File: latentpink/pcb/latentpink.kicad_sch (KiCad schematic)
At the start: 20 parts, among them M10 WEEE, M3 SCREWHOLE, M4 SCREWHOLE, M5 SCREWHOLE, M6 SCREWHOLE, M7 LONGTHING, M8 OSHW, M9 POLARITY

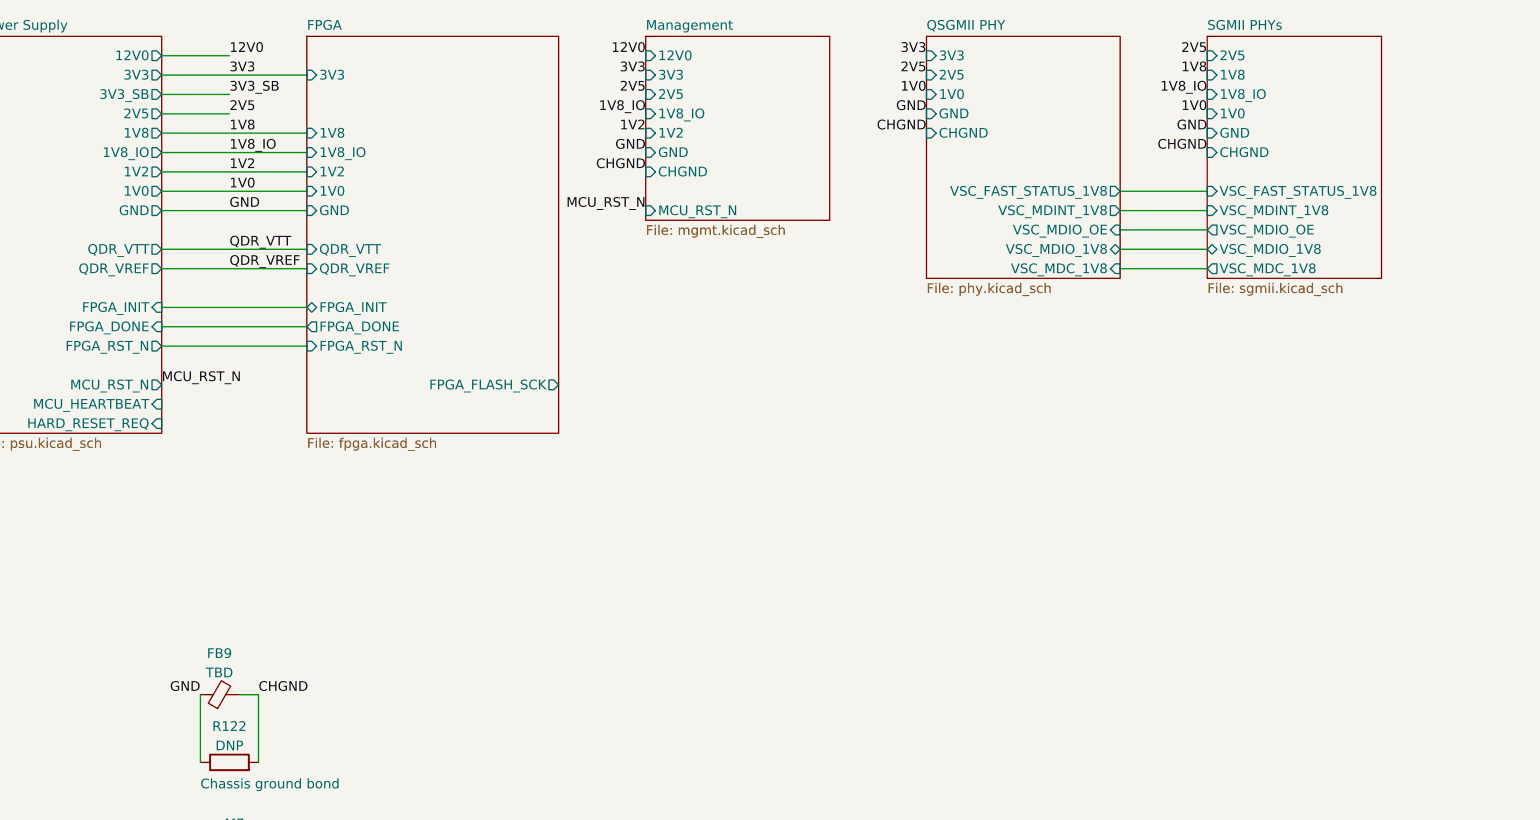
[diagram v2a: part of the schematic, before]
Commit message: Finished initial schematic, ready for design review
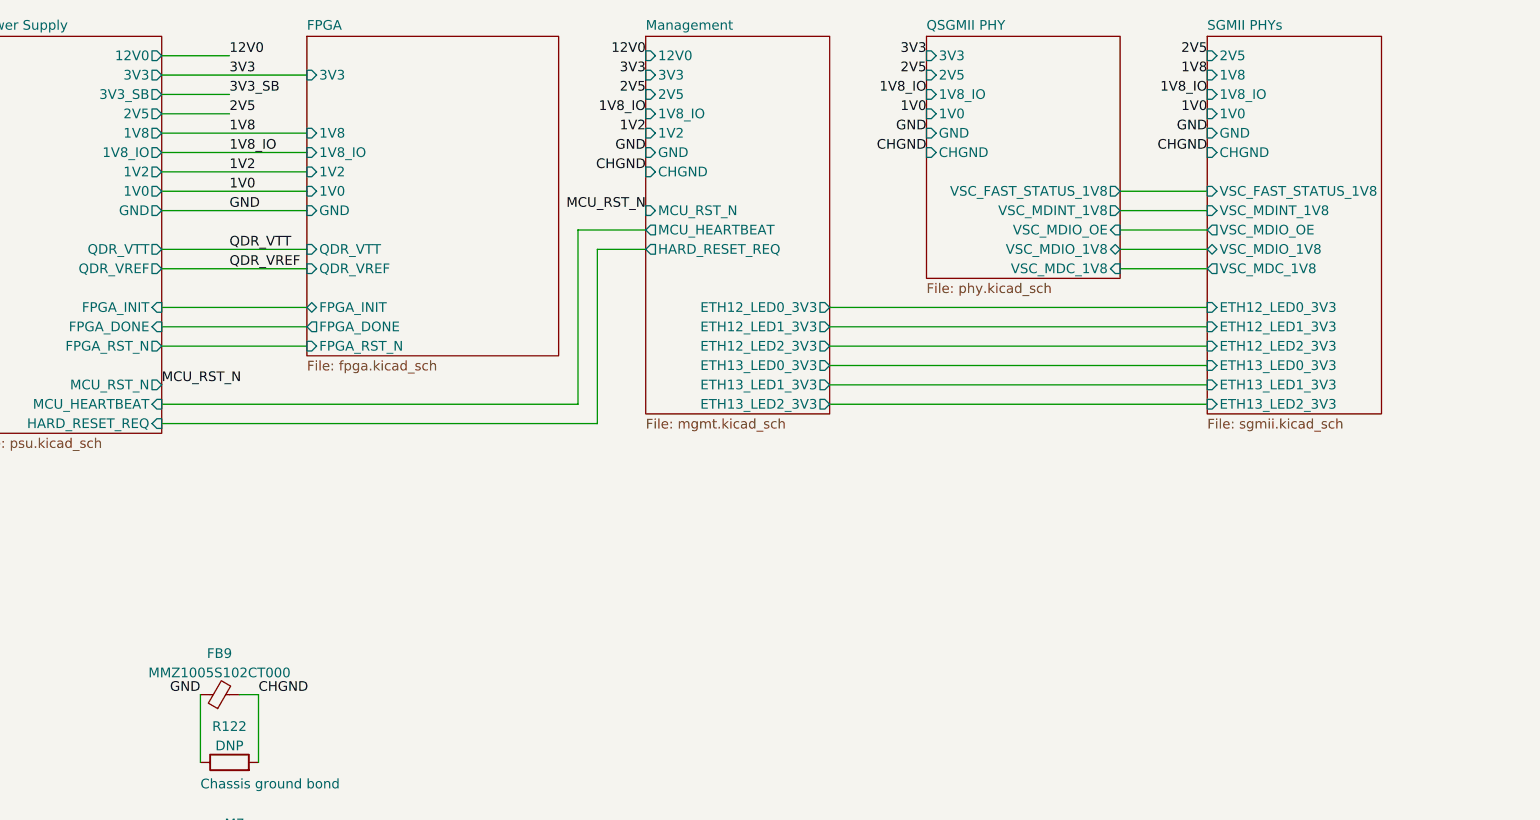
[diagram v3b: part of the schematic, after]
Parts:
- FB9: value TBD -> MMZ1005S102CT000; footprint (none) -> azonenberg_pcb:EIA_0402_CAP_NOSILK
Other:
- sheet FPGA ports: added none; removed FPGA_FLASH_SCK
- sheet Management ports: added ETH12_LED0_3V3, ETH12_LED1_3V3, ETH12_LED2_3V3, ETH13_LED0_3V3, ETH13_LED1_3V3, ETH13_LED2_3V3, HARD_RESET_REQ, MCU_HEARTBEAT; removed none
- sheet QSGMII PHY ports: added 1V8_IO; removed none
- sheet SGMII PHYs ports: added ETH12_LED0_3V3, ETH12_LED1_3V3, ETH12_LED2_3V3, ETH13_LED0_3V3, ETH13_LED1_3V3, ETH13_LED2_3V3; removed none

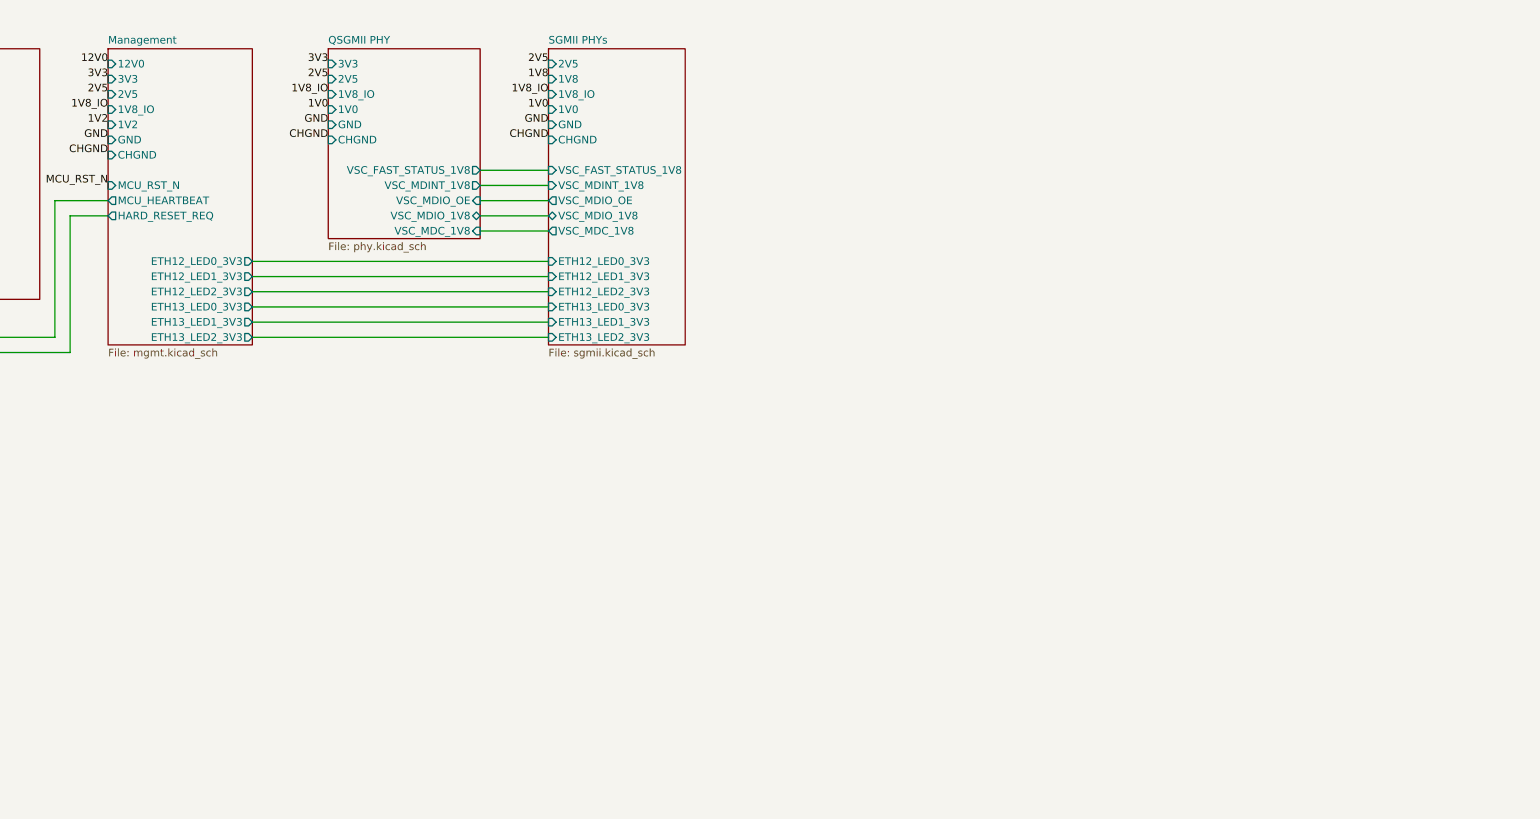
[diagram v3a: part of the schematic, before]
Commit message: Added some debug LEDs, PMOD, and temp sensors
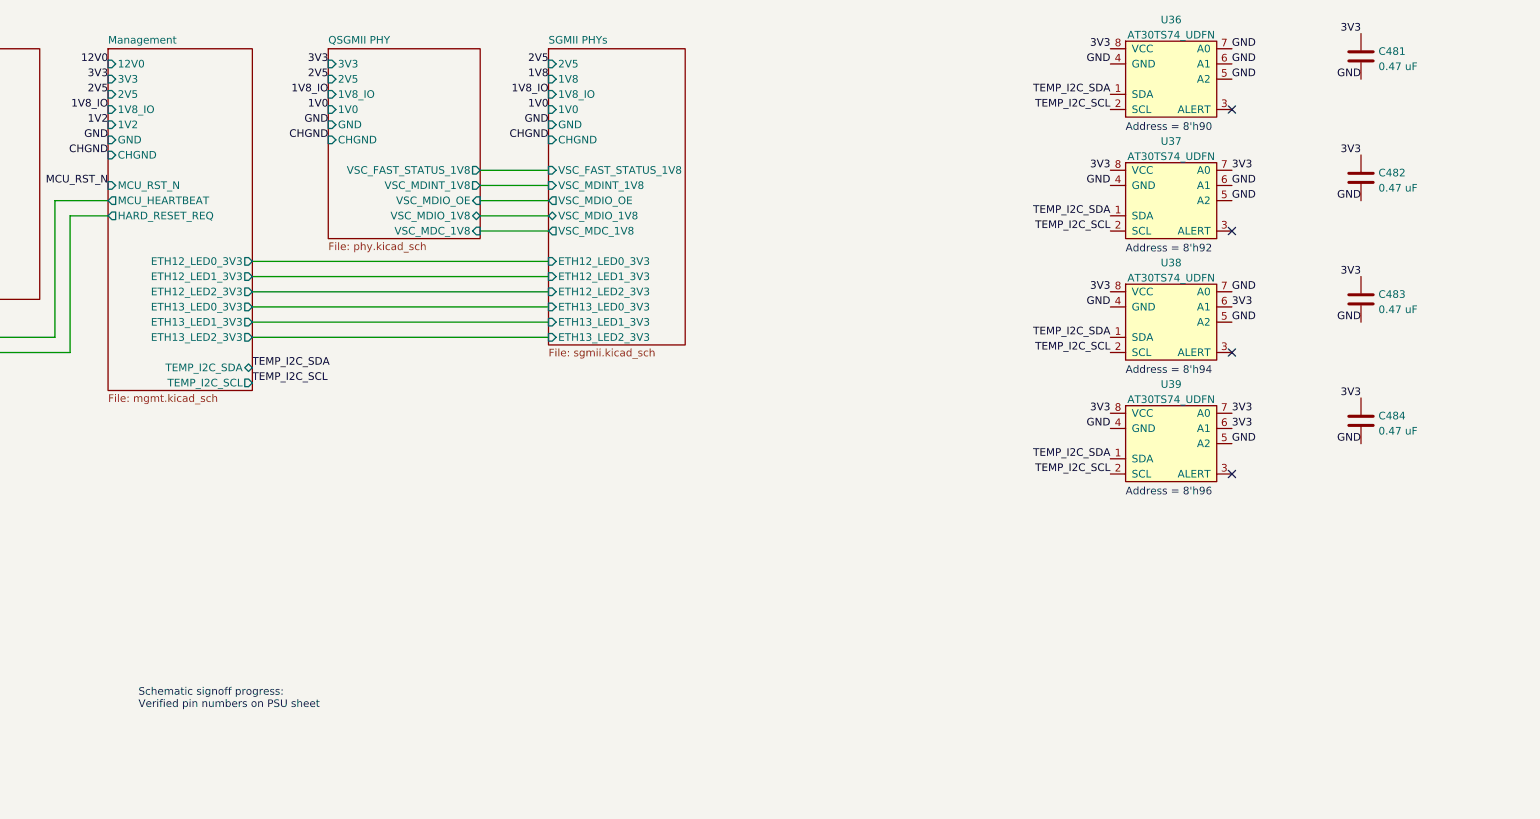
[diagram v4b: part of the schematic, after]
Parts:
- added C481, C482, C483, C484: 0.47 uF, azonenberg_pcb:EIA_0402_CAP_NOSILK, symbol device:C
- added U36, U37, U38, U39: AT30TS74_UDFN, azonenberg_pcb:DFN_8_0.5MM_2x3MM_TALL, symbol special-azonenberg:AT30TS74_UDFN
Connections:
- net 3V3: now also C481.1, C482.1, C483.1, C484.1, U36.8 (VCC), U37.7 (A0), U37.8 (VCC), U38.6 (A1), U38.8 (VCC), U39.6 (A1), U39.7 (A0), U39.8 (VCC)
- net GND: now also C481.2, C482.2, C483.2, C484.2, U36.4 (GND), U36.5 (A2), U36.6 (A1), U36.7 (A0), U37.4 (GND), U37.5 (A2), U37.6 (A1), U38.4 (GND), U38.5 (A2), U38.7 (A0), U39.4 (GND), U39.5 (A2)
- new net TEMP_I2C_SCL: U36.2 (SCL), U37.2 (SCL), U38.2 (SCL), U39.2 (SCL)
- new net TEMP_I2C_SDA: U36.1 (SDA), U37.1 (SDA), U38.1 (SDA), U39.1 (SDA)
- no-connect marks 0 -> 4
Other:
- sheet Management ports: added TEMP_I2C_SCL, TEMP_I2C_SDA; removed none
- note added: "Address = 8'h90"
- note added: "Address = 8'h92"
- note added: "Address = 8'h94"
- note added: "Address = 8'h96"
- note added: "Schematic signoff progress: Verified pin numbers on PSU sheet"
